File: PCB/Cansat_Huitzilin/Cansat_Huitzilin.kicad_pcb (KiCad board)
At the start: 4 copper layers, 59 x 59 mm, 71 parts, among them IC1 AP64501SP-13, IC2 114993390, IC3 BMM350, IC4 BMI323, IC5 STCC4-D-R3, IC6 SHT40-AD1B-R2, J1 Screw_Terminal_01x02, J2 Conn_01x04, J3 Conn_01x03, J4 Conn_01x06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

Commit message: Actualización del diseño PCB
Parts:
- added J7: Conn_01x04, Connector_PinHeader_2.54mm:PinHeader_1x04_P2.54mm_Vertical, F.Cu at (42.0, 44.8)
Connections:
- U1 pad 27: unconnected-(U1-IO47-Pad27) -> TX_PI
- U1 pad 30: unconnected-(U1-IO48-Pad30) -> RX_PI
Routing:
- net DIO1: track 0.00 -> 55.7 mm, vias 0 -> 6
- net BUSY: track 0.00 -> 53.6 mm, vias 0 -> 4
- net MOSI: track 33.7 -> 83.9 mm, vias 2 -> 6
- net SCK: track 38.2 -> 82.3 mm, vias 2 -> 6
- net MISO: track 38.4 -> 81.3 mm, vias 2 -> 3
- net RX_PI: track 0.00 -> 32.6 mm, vias 0 -> 4
- net TX_PI: track 0.00 -> 23.0 mm, vias 0 -> 2
- net BOOT: track 43.6 -> 43.0 mm

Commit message: PCB-m
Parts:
- moved R10 59.1 mm to (111.9, 70.8), turned to 90 degrees
- moved J1 54.9 mm to (84.2, 91.4)
- moved C1 54.9 mm to (78.3, 83.5)
- moved C10 54.9 mm to (82.2, 52.6)
- moved C11 54.9 mm to (82.2, 51.0)
- moved C12 54.9 mm to (76.3, 48.6)
- moved C13 54.9 mm to (88.0, 54.4)
- moved C15 54.9 mm to (110.6, 64.0)
- moved C16 54.9 mm to (102.8, 80.7)
- moved C17 54.9 mm to (95.0, 92.0)
- moved C18 54.9 mm to (101.0, 92.0)
- moved C20 54.9 mm to (115.0, 93.8)
- moved C21 54.9 mm to (108.2, 94.0)
- moved C23 54.9 mm to (105.5, 91.2)
- moved C25 54.9 mm to (84.2, 44.6)
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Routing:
- net MOSI: track 83.9 -> 72.6 mm, vias 6 -> 3
- net MISO: track 81.3 -> 71.1 mm
- net SDA: track 81.6 -> 88.8 mm
- net RX_PI: track 32.6 -> 25.5 mm, vias 4 -> 1
- net CS_SD: track 27.4 -> 20.6 mm
- net NRST: track 42.4 -> 35.7 mm, vias 4 -> 2
- net SERVO 1: track 38.6 -> 44.5 mm, vias 2 -> 1
- net BUSY: track 53.6 -> 48.9 mm, vias 4 -> 2
- net BOOT: track 43.0 -> 47.4 mm
- net SCK: track 82.3 -> 78.7 mm, vias 6 -> 5
- net TX_PI: track 23.0 -> 20.1 mm, vias 2 -> 1
- net Enable ESP: track 29.6 -> 31.9 mm
- net RX: track 23.0 -> 24.5 mm, vias 3 -> 1
- net +3.3V: track 55.8 -> 57.0 mm
- net TX_GPS: track 43.6 -> 44.8 mm
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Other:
- rule pad_to_mask_clearance: 0 -> 0.1

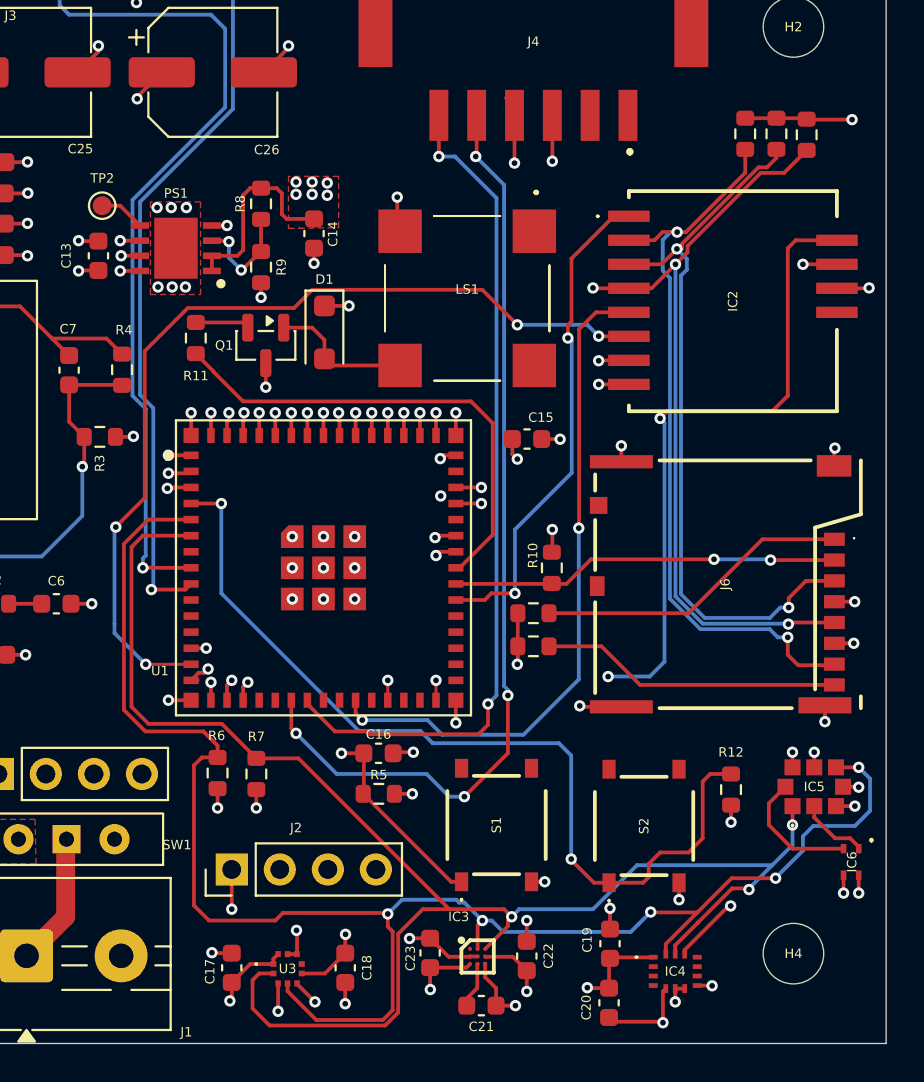
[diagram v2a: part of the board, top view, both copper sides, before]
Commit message: PCB
Modify the track spacing
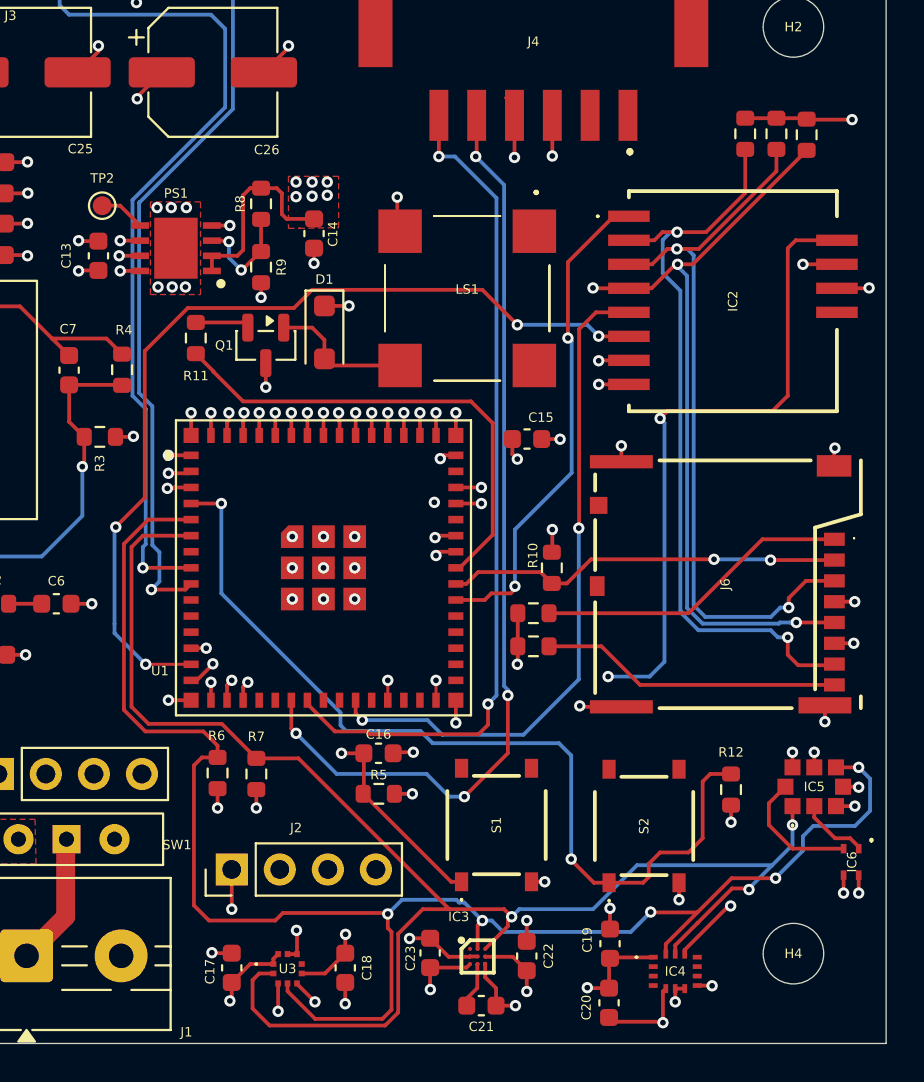
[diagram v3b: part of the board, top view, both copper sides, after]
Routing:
- net RX: track 24.5 -> 28.6 mm
- net MISO: track 71.1 -> 71.9 mm
